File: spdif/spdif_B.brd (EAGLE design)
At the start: 80 x 80 mm, 66 parts, among them T1 DA101MC, T2 DA101MC, U1 NC7SZ175, U2 FIN1001, U3 FIN1002, U4 NC7SZ175, U5 NC7SZ175, U6 FIN1002

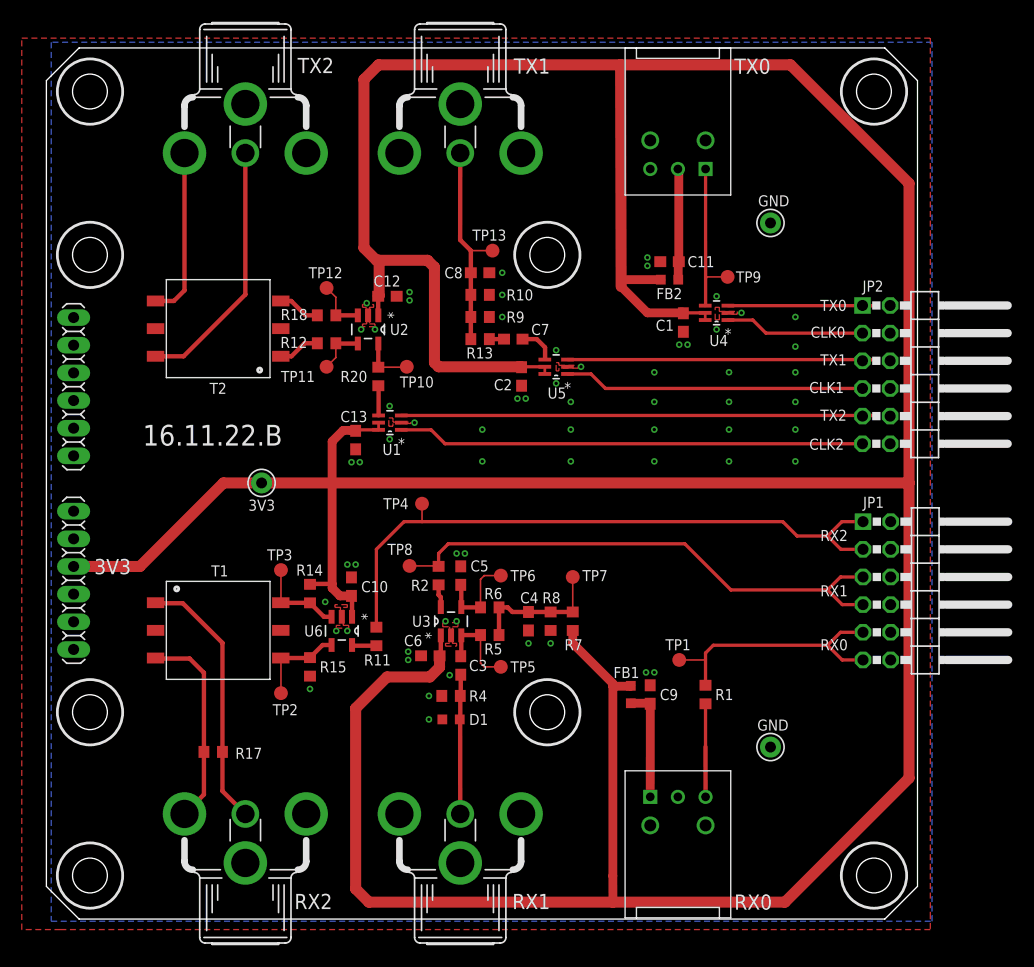
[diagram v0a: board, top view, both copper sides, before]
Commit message: spdif: updated new liwe conn + minor tweaks.
Signed-off-by: malo <pavol.malosek@gmail.com>
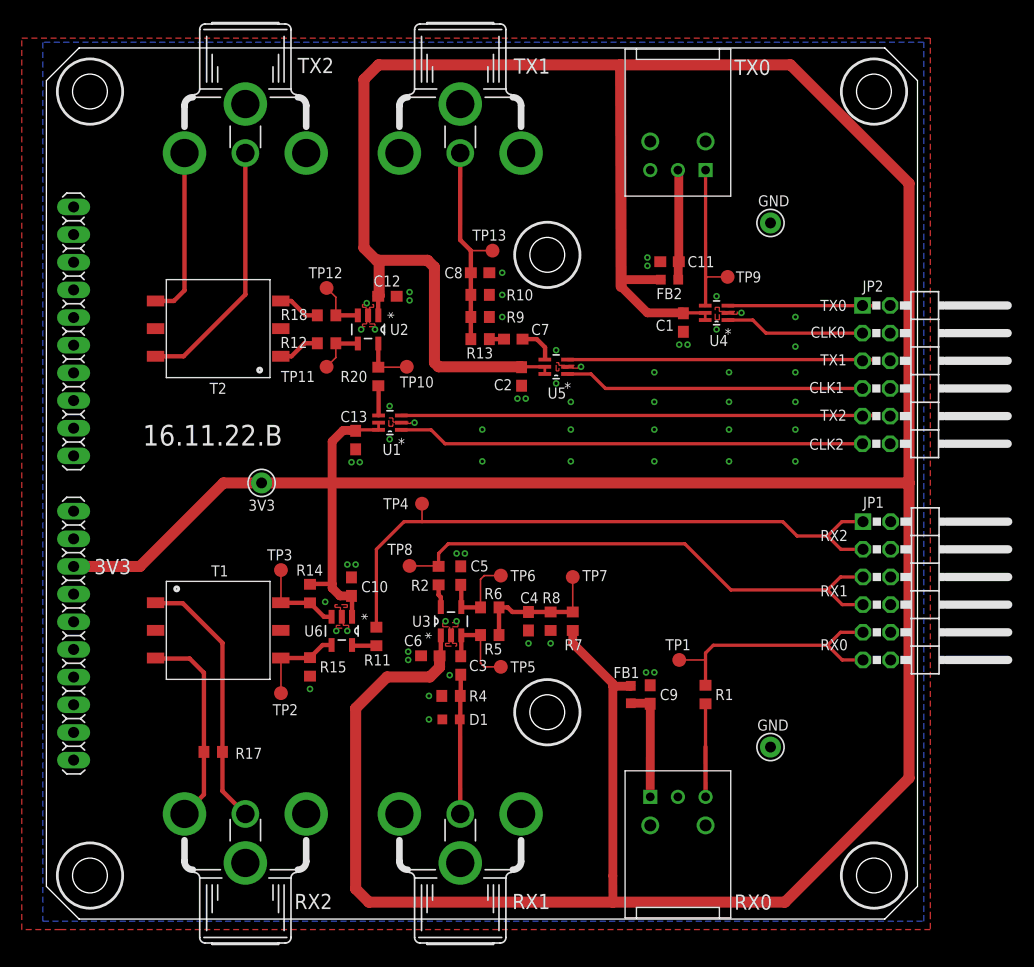
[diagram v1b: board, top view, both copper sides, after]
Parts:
- moved TX0 0.10 mm to (58.0, 68.8)
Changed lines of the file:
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@@
 <setting verticaltext="up"/>
 </settings>
-<grid distance="10" unitdist="mil" unit="mil" style="lines" multiple="1" display="yes" altdistance="0.025" altunitdist="inch" altunit="inch"/>
+<grid distance="10" unitdist="mil" unit="mil" style="lines" multiple="1" display="no" altdistance="0.025" altunitdist="inch" altunit="inch"/>
 <layers>
 <layer number="1" name="Top" color="4" fill="1" visible="yes" active="yes"/>
@@
 <attribute name="NAME" x="63.325" y="58.467" size="1.016" layer="25" font="vector" ratio="15"/>
 </element>
-<element name="TX0" library="25cmsquare" package="PLT133_T10W" value="PLT133/T10W" x="57.9976" y="68.8848" smashed="yes">
-<attribute name="NAME" x="63.1792" y="77.6224" size="1.397" layer="21" font="vector" ratio="15"/>
+<element name="TX0" library="25cmsquare" package="PLT133_T10W" value="PLT133/T10W" x="57.9976" y="68.7832" smashed="yes">
+<attribute name="NAME" x="63.1792" y="77.5208" size="1.397" layer="21" font="vector" ratio="15"/>
 </element>
 <element name="TX1" library="25cmsquare" package="RCJ-01X" value="RCJ-01X, CP-1400-ND" x="38.0078" y="70.35" smashed="yes">
@@
 <contactref element="GND33" pad="1"/>
 <polygon width="0.1524" layer="16">
-<vertex x="0.4412" y="80.518"/>
-<vertex x="0.4412" y="-0.2032"/>
-<vertex x="81.3402" y="-0.2032"/>
-<vertex x="81.3402" y="80.518"/>
+<vertex x="-0.3208" y="80.518"/>
+<vertex x="-0.3208" y="-0.2032"/>
+<vertex x="80.5782" y="-0.2032"/>
+<vertex x="80.5782" y="80.518"/>
 </polygon>
 <polygon width="0.1524" layer="1">
@@
 <contactref element="TP9" pad="TP"/>
 <contactref element="TX0" pad="1"/>
-<wire x1="60.5376" y1="68.8848" x2="60.54" y2="58.848" width="0.3048" layer="1"/>
+<wire x1="60.5376" y1="68.7832" x2="60.54" y2="58.848" width="0.3048" layer="1"/>
 <wire x1="60.54" y1="58.848" x2="60.54" y2="56.3678" width="0.3048" layer="1"/>
 <wire x1="60.54" y1="56.3678" x2="60.5056" y2="56.3334" width="0.3048" layer="1"/>
@@
 <wire x1="58.029" y1="60.322" x2="58.079" y2="60.372" width="0.8128" layer="1"/>
 <wire x1="58.079" y1="60.372" x2="58.079" y2="68.8034" width="0.8128" layer="1"/>
-<wire x1="58.079" y1="68.8034" x2="57.9976" y2="68.8848" width="0.8128" layer="1"/>
+<wire x1="58.079" y1="68.8034" x2="57.9976" y2="68.7832" width="0.8128" layer="1"/>
 </signal>
 <signal name="CLK_0">

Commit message: spdif: B variant PCB finished
Signed-off-by: malo <pavol.malosek@gmail.com>
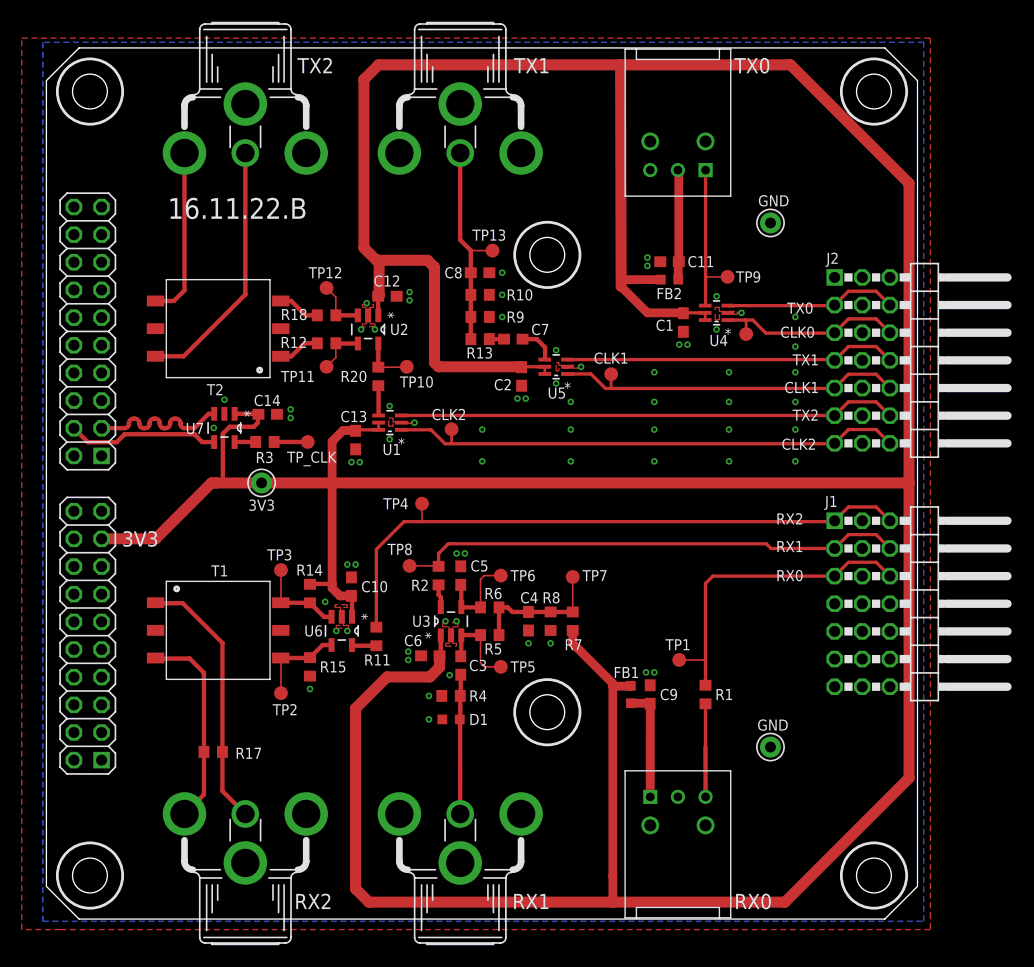
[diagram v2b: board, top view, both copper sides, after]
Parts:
- removed JP1, JP2: (no value), 25pinhead:2X06/90
- removed PWR: (no value), 25cmsquare:LIWE_12_PIN_8X8_COMPAT
- added C14: 100n, 0603, rcl:C0603
- added CLK0, CLK1, CLK2, TP_CLK: TPB1,27, testpad:B1,27
- added J1, J2: PINHD-3X7/90, 25pinhead:3X07/90
- added R3: , 0603, rcl:R0603
- added U$2: LIWE_40_PIN, 25cmsquare:LIWE_40_PIN_8X8
- added U7: FIN1002, 25cmsquare:SOT95P280X140-5N
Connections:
- new net CLK_N: U$2.104, U7.4
- new net CLK_P: U$2.103, U7.3
- new net N$10: R3.1, TP_CLK.TP
- new net N$9: R3.2, U7.5
- net +1V0: now also U$2.13; no longer PWR.2
- net +2V5: now also U$2.15; no longer PWR.1
- net +3V3: now also C14.2, U$2.17, U7.1; no longer PWR.4
- net +5V: now also U$2.19; no longer PWR.6
- net CLK_0: now also CLK0.TP, J2.7, J2.9; no longer JP2.3
- net CLK_1: now also CLK1.TP, J2.13, J2.15; no longer JP2.7
- net CLK_2: now also CLK2.TP, J2.19, J2.21; no longer JP2.11
- net GND: now also C14.1, J1.11, J1.14, J1.17, J1.2, J1.20, J1.5, J1.8, J2.11, J2.14, J2.17, J2.2, J2.20, J2.5, J2.8, U$2.18, U7.2; no longer JP1.10, JP1.12, JP1.2, JP1.4, JP1.6, JP1.8, JP2.10, JP2.12, JP2.2, JP2.4, JP2.6, JP2.8, PWR.3, PWR.8
- net SPDIF_IN_0: now also J1.7, J1.9; no longer JP1.11, JP1.9
- net SPDIF_IN_1: now also J1.4, J1.6; no longer JP1.5, JP1.7
- net SPDIF_IN_2: now also J1.1, J1.3; no longer JP1.1, JP1.3
- net SPDIF_OUT_0: now also J2.4, J2.6; no longer JP2.1
- net SPDIF_OUT_1: now also J2.10, J2.12; no longer JP2.5
- net SPDIF_OUT_2: now also J2.16, J2.18; no longer JP2.9
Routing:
- net CLK_N: track 0.00 -> 14.0 mm
- net CLK_P: track 0.00 -> 13.3 mm
- net +3V3: track 410.1 -> 421.9 mm
- net SPDIF_IN_0: track 24.4 -> 30.0 mm
- net CLK_2: track 42.9 -> 47.8 mm
- net CLK_0: track 12.9 -> 17.8 mm
- net CLK_1: track 27.6 -> 32.6 mm
- net N$10: track 0.00 -> 3.09 mm
- net SPDIF_IN_1: track 49.3 -> 46.9 mm
- net N$9: track 0.00 -> 1.93 mm
- net SPDIF_OUT_1: track 28.9 -> 30.7 mm
- net SPDIF_OUT_2: track 44.2 -> 45.9 mm
- net SPDIF_OUT_0: track 14.3 -> 16.0 mm
- net SPDIF_IN_2: track 59.4 -> 58.1 mm

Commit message: spdif: added diff signaling for TX/RX 2
Signed-off-by: malo <pavol.malosek@gmail.com>
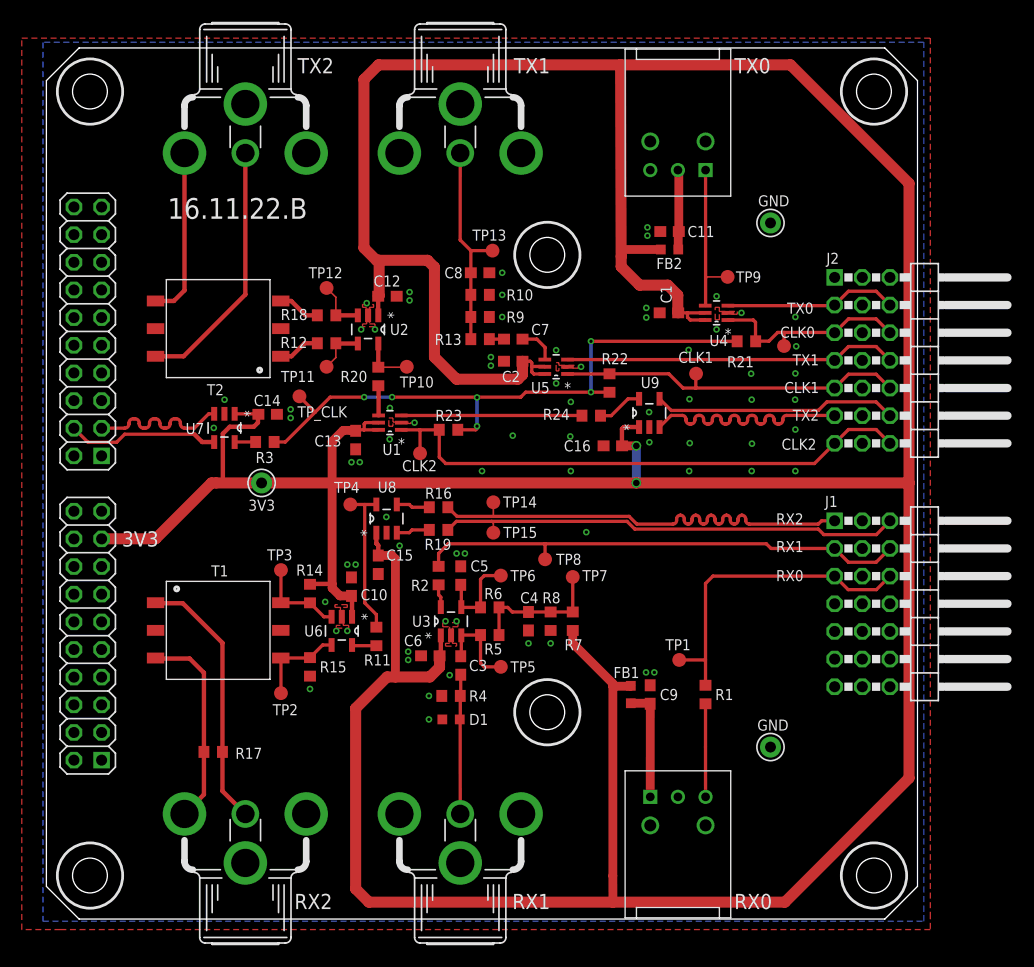
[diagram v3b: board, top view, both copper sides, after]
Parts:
- added C15, C16: 100n, 0603, rcl:C0603
- added R16, R19, R21, R22, R23, R24: 22R, 0603, rcl:R0603
- added TP14, TP15: TPB1,27, testpad:B1,27
- added U8: FIN1001, 25cmsquare:SOT95P280X140-5N
- added U9: FIN1002, 25cmsquare:SOT95P280X140-5N
- moved TP8 12.5 mm to (45.8, 33.0)
- moved CLK1 7.80 mm to (59.7, 50.1)
- moved TP4 6.58 mm to (27.9, 38.1)
- moved TP_CLK 4.26 mm to (23.2, 48.0)
- moved CLK0 3.65 mm to (67.7, 52.6)
- moved CLK2 3.64 mm to (34.3, 42.8)
- moved FB2 2.77 mm to (57.2, 61.5)
- moved C11 2.77 mm to (57.2, 63.1)
- moved C1 1.60 mm to (57.2, 55.7), turned to 0 degrees
- moved C2 1.60 mm to (42.9, 51.2), turned to 0 degrees
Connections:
- net N$7 renamed U6_OUT
- removed net SPDIF_IN_2: J1.1, J1.3, R11.2, TP4.TP
- removed net SPDIF_OUT_2: J2.16, J2.18, U1.3
- new net CLK_IN: R21.2, R22.2, R23.2, R3.1, TP_CLK.TP
- new net N$1: R11.2, TP4.TP, U8.5
- new net N$2: R16.1, U8.4
- new net N$7: R19.1, U8.3
- new net N$8: R24.2, U9.5
- new net SPDIF_IN_2_N: J1.3, R19.2, TP15.TP
- new net SPDIF_IN_2_P: J1.1, R16.2, TP14.TP
- new net SPDIF_OUT_2_N: J2.18, U9.4
- new net SPDIF_OUT_2_P: J2.16, U9.3
- net +3V3: now also C15.2, C16.2, U8.1, U9.1
- net CLK_0: now also R21.1
- net CLK_1: now also R22.1
- net CLK_2: now also R23.1
- net GND: now also C15.1, C16.1, U8.2, U9.2
- net N$10: now also R24.1, U1.3; no longer R3.1, TP_CLK.TP
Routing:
- net SPDIF_IN_2: track 58.1 -> 0.00 mm
- net CLK_IN: track 0.00 -> 57.5 mm, vias 0 -> 6
- net SPDIF_OUT_2: track 45.9 -> 0.00 mm
- net SPDIF_IN_2_N: track 0.00 -> 43.1 mm
- net SPDIF_IN_2_P: track 0.00 -> 41.7 mm
- net +3V3: track 421.9 -> 450.0 mm, vias 0 -> 2
- net SPDIF_OUT_2_N: track 0.00 -> 22.5 mm
- net SPDIF_OUT_2_P: track 0.00 -> 21.2 mm
- net N$1: track 0.00 -> 15.2 mm
- net N$10: track 3.09 -> 16.6 mm
- net N$8: track 0.00 -> 4.19 mm
- net CLK_2: track 47.8 -> 51.7 mm
- net N$7: track 0.00 -> 3.09 mm
- net N$2: track 0.00 -> 3.09 mm
- net TX0_VCC: track 10.2 -> 7.42 mm
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
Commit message: spdif: final tweaks
Signed-off-by: malo <pavol.malosek@gmail.com>
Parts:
- added C17: 10u, rcl:C0805
- added FB3: (no value), 25cmsquare:L0603
- added TP16, TP17, TP18, TP19, TP20: TPB1,27, testpad:B1,27
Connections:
- removed net +1V0: U$2.13
- removed net +2V5: U$2.15
- removed net +5V: U$2.19
- new net N$14: J1.10, TP17.TP
- new net N$18: J1.13, TP18.TP
- new net N$19: J1.16, TP19.TP
- new net N$22: J1.19, TP20.TP
- new net N$23: FB3.1, U$2.17
- net +3V3: now also C17.2, FB3.2; no longer U$2.17
- net GND: now also C17.1
- net N$10: now also TP16.TP
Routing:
- net N$23: track 0.00 -> 6.76 mm
- net +3V3: track 450.0 -> 444.5 mm
- net N$22: track 0.00 -> 3.12 mm
- net N$19: track 0.00 -> 3.12 mm
- net N$18: track 0.00 -> 3.12 mm
- net N$14: track 0.00 -> 3.12 mm
- net N$10: track 16.6 -> 18.2 mm
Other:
- board text added: "25"
